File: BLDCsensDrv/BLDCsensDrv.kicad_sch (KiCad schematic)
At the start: 31 parts, among them J1 Screw_Terminal_01x02, J3 Screw_Terminal_01x03, Q1 IRF540N, Q2 IRF540N, Q3 IRF540N, Q4 IRF540N, Q5 IRF540N, Q6 IRF540N, U1 MCT8329A1IREER

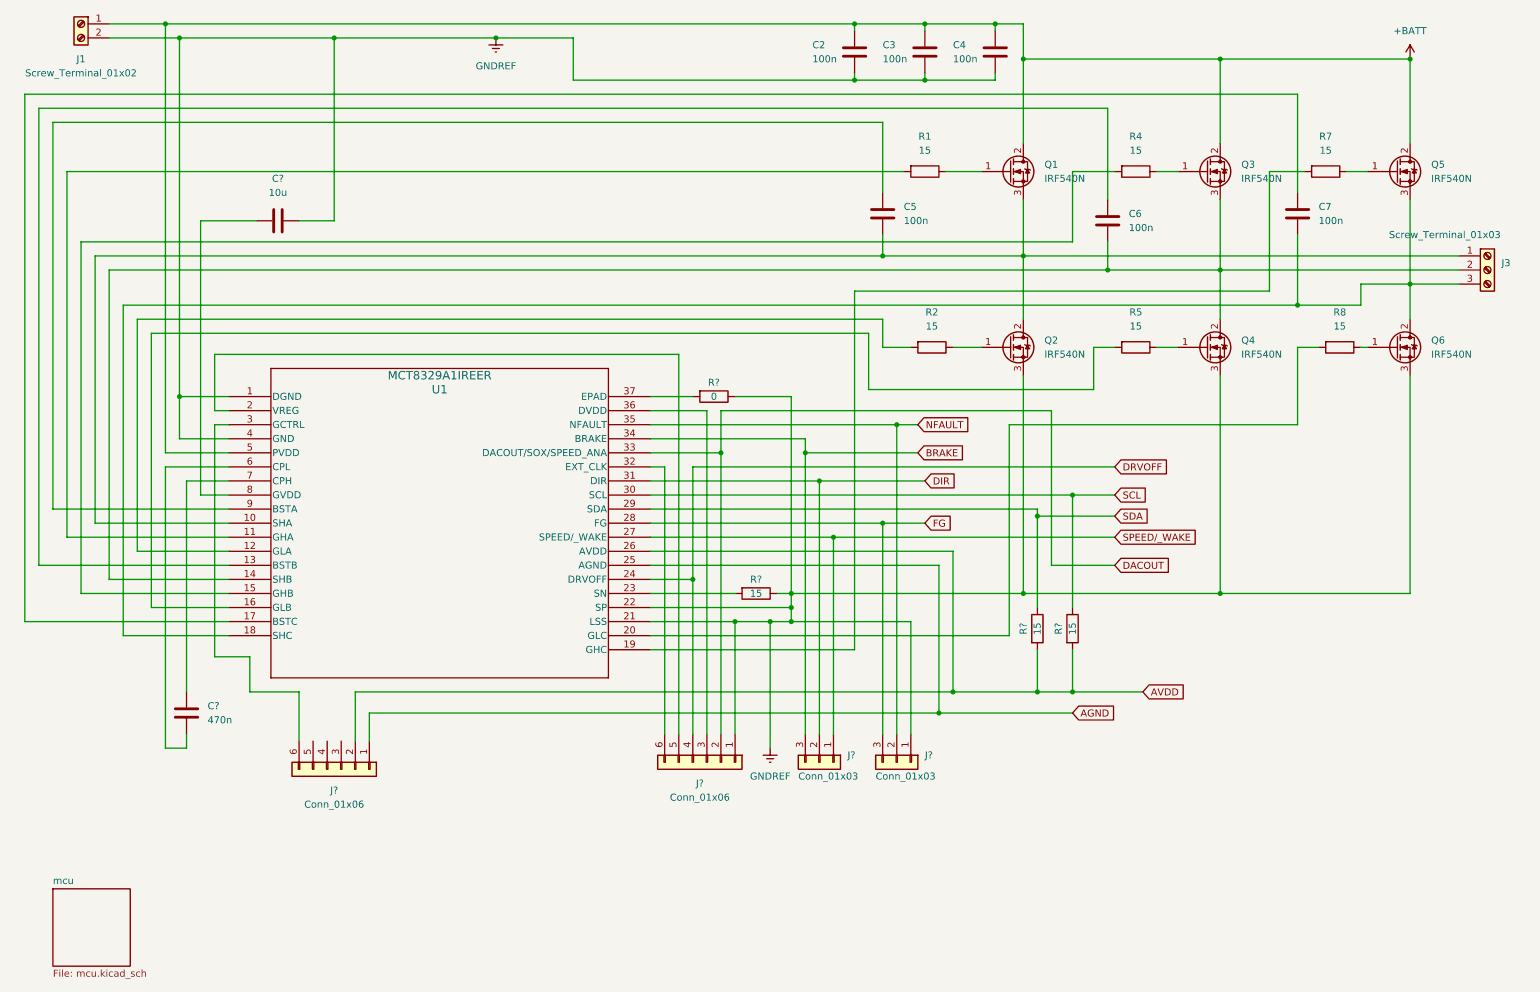
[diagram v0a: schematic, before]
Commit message: 3-phase Trapezoidal Control hardware ready for prototype prod.
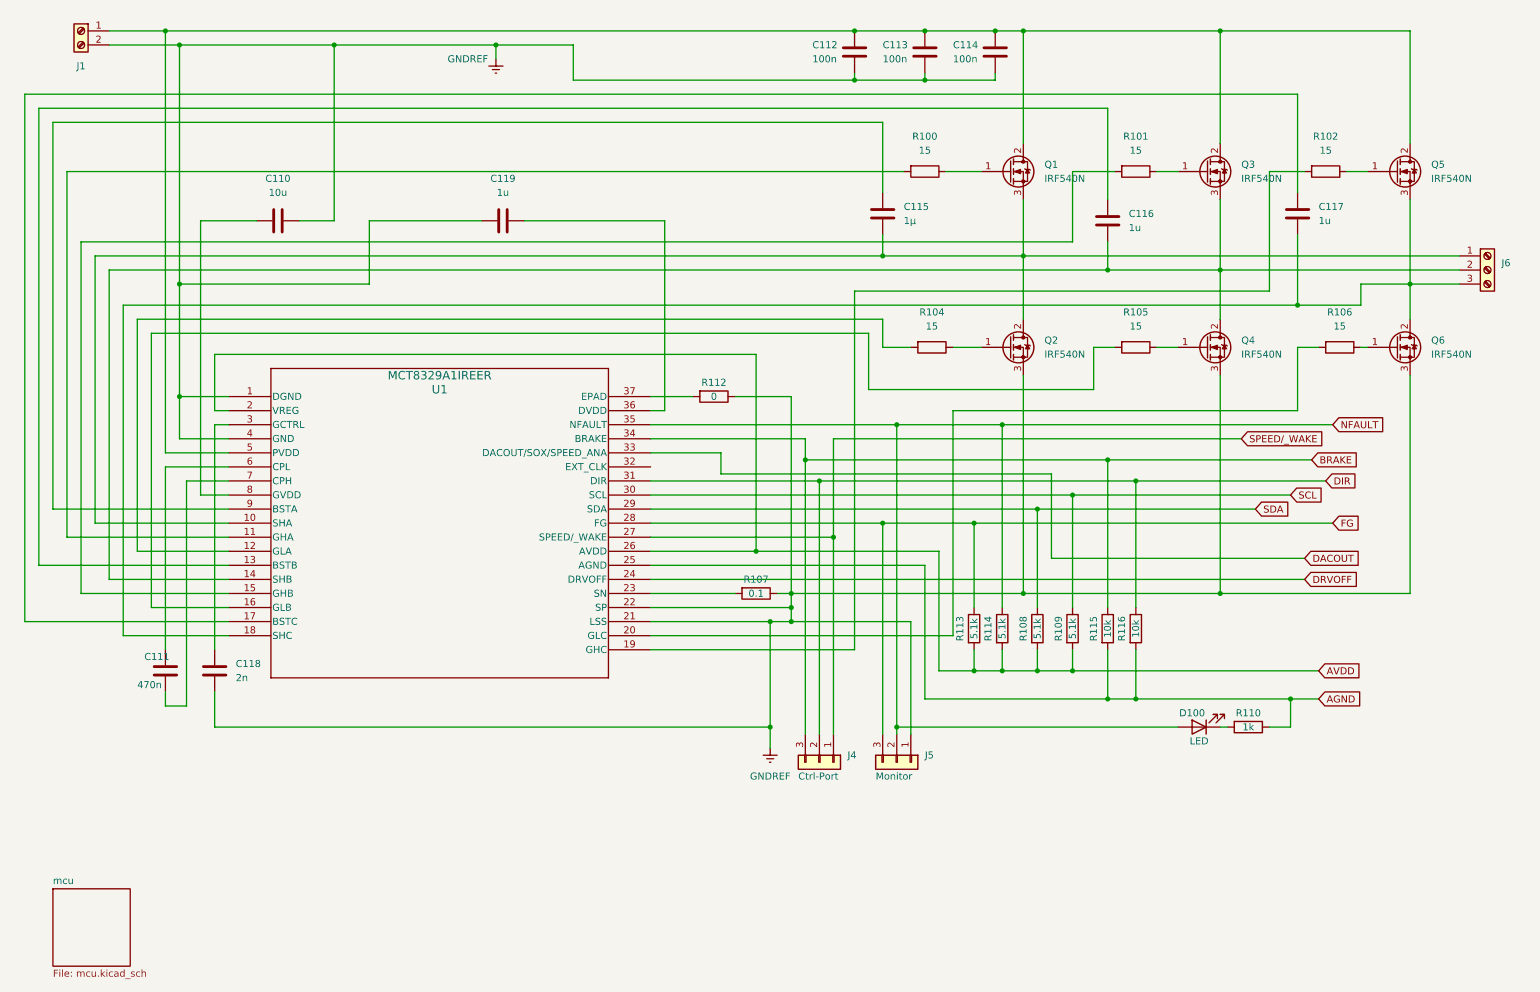
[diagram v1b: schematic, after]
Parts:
- removed C?: 470n, Capacitor_THT:C_Axial_L3.8mm_D2.6mm_P7.50mm_Horizontal, symbol Device:C
- removed J? (x2): Conn_01x06, symbol Connector_Generic:Conn_01x06
- added C111: 470n, Capacitor_SMD:C_1206_3216Metric_Pad1.33x1.80mm_HandSolder, symbol Device:C
- added C118: 2n, Capacitor_SMD:C_1206_3216Metric_Pad1.33x1.80mm_HandSolder, symbol Device:C
- added C119: 1u, Capacitor_SMD:C_1206_3216Metric_Pad1.33x1.80mm_HandSolder, symbol Device:C
- added D100: LED, LED_SMD:LED_1206_3216Metric_Pad1.42x1.75mm_HandSolder, symbol Device:LED
- added R110: 1k, Resistor_SMD:R_1206_3216Metric_Pad1.30x1.75mm_HandSolder, symbol Device:R
- added R113, R114: 5.1k, Resistor_SMD:R_1206_3216Metric_Pad1.30x1.75mm_HandSolder, symbol Device:R
- added R115, R116: 10k, Resistor_SMD:R_1206_3216Metric_Pad1.30x1.75mm_HandSolder, symbol Device:R
- C110: renamed from C?; footprint Capacitor_THT:C_Axial_L3.8mm_D2.6mm_P7.50mm_Horizontal -> Capacitor_SMD:C_1206_3216Metric_Pad1.33x1.80mm_HandSolder
- C112: renamed from C2; footprint Capacitor_THT:C_Axial_L3.8mm_D2.6mm_P7.50mm_Horizontal -> Capacitor_SMD:C_1206_3216Metric_Pad1.33x1.80mm_HandSolder
- C113: renamed from C3; footprint Capacitor_THT:C_Axial_L3.8mm_D2.6mm_P7.50mm_Horizontal -> Capacitor_SMD:C_1206_3216Metric_Pad1.33x1.80mm_HandSolder
- C114: renamed from C4; footprint Capacitor_THT:C_Axial_L3.8mm_D2.6mm_P7.50mm_Horizontal -> Capacitor_SMD:C_1206_3216Metric_Pad1.33x1.80mm_HandSolder
- C115: renamed from C5; value 100n -> 1µ; footprint Capacitor_THT:C_Axial_L3.8mm_D2.6mm_P7.50mm_Horizontal -> Capacitor_SMD:C_1206_3216Metric_Pad1.33x1.80mm_HandSolder
- C116: renamed from C6; value 100n -> 1u; footprint Capacitor_THT:C_Axial_L3.8mm_D2.6mm_P7.50mm_Horizontal -> Capacitor_SMD:C_1206_3216Metric_Pad1.33x1.80mm_HandSolder
- C117: renamed from C7; value 100n -> 1u; footprint Capacitor_THT:C_Axial_L3.8mm_D2.6mm_P7.50mm_Horizontal -> Capacitor_SMD:C_1206_3216Metric_Pad1.33x1.80mm_HandSolder
- J4: renamed from J?; value Conn_01x03 -> Ctrl-Port; footprint (none) -> Connector_PinHeader_2.54mm:PinHeader_1x03_P2.54mm_Vertical
- J5: renamed from J?; value Conn_01x03 -> Monitor; footprint (none) -> Connector_PinHeader_2.54mm:PinHeader_1x03_P2.54mm_Vertical
- R100: renamed from R1; footprint Resistor_THT:R_Axial_DIN0207_L6.3mm_D2.5mm_P10.16mm_Horizontal -> Resistor_SMD:R_1206_3216Metric_Pad1.30x1.75mm_HandSolder
- R101: renamed from R4; footprint Resistor_THT:R_Axial_DIN0207_L6.3mm_D2.5mm_P10.16mm_Horizontal -> Resistor_SMD:R_1206_3216Metric_Pad1.30x1.75mm_HandSolder
- R102: renamed from R7; footprint Resistor_THT:R_Axial_DIN0207_L6.3mm_D2.5mm_P10.16mm_Horizontal -> Resistor_SMD:R_1206_3216Metric_Pad1.30x1.75mm_HandSolder
- R104: renamed from R2; footprint Resistor_THT:R_Axial_DIN0207_L6.3mm_D2.5mm_P10.16mm_Horizontal -> Resistor_SMD:R_1206_3216Metric_Pad1.30x1.75mm_HandSolder
- R105: renamed from R5; footprint Resistor_THT:R_Axial_DIN0207_L6.3mm_D2.5mm_P10.16mm_Horizontal -> Resistor_SMD:R_1206_3216Metric_Pad1.30x1.75mm_HandSolder
- R106: renamed from R8; footprint Resistor_THT:R_Axial_DIN0207_L6.3mm_D2.5mm_P10.16mm_Horizontal -> Resistor_SMD:R_1206_3216Metric_Pad1.30x1.75mm_HandSolder
- R107: renamed from R?; value 15 -> 0.1; footprint Resistor_THT:R_Axial_DIN0207_L6.3mm_D2.5mm_P10.16mm_Horizontal -> Resistor_SMD:R_1206_3216Metric_Pad1.30x1.75mm_HandSolder
- R108, R109: renamed from R?; value 15 -> 5.1k; footprint Resistor_THT:R_Axial_DIN0207_L6.3mm_D2.5mm_P10.16mm_Horizontal -> Resistor_SMD:R_1206_3216Metric_Pad1.30x1.75mm_HandSolder
- R112: renamed from R?; footprint Resistor_THT:R_Axial_DIN0207_L6.3mm_D2.5mm_P10.16mm_Horizontal -> Resistor_SMD:R_1206_3216Metric_Pad1.30x1.75mm_HandSolder
- renumbered J3 to J6
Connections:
- net AGND: now also R110.1, R115.2, R116.2
- net AVDD: now also U1.2 (VREG), R113.2, R114.2
- net BRAKE: now also R115.1
- net DIR: now also R116.1
- net FG: now also R113.1
- net GNDREF: now also C118.2, C119.1
- net NFAULT: now also D100.2 (A), R114.1
- net at U1.7 (CPH): now also C111.2
- net at U1.6 (CPL): now also C111.1
- net at U1.3 (GCTRL): now also C118.1
- net at U1.36 (DVDD): now also C119.2
- net +BATT: no longer names the net of C112.1, C113.1, C114.1, J1.1 (Pin_1), Q1.2 (D), Q3.2 (D), Q5.2 (D), U1.5 (PVDD)
- new net: D100.1 (K), R110.2
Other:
- moved on the sheet: J1

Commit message: Hasty checkin of current development projects...
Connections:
- net PVDD: now reaches C112.1, C113.1, C114.1, J1.1 (Pin_1), Q1.2 (D), Q3.2 (D), Q5.2 (D), U1.5 (PVDD)
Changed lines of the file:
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@@
+	)
+	(junction
+		(at 40.64 27.94)
+		(diameter 0)
+		(color 0 0 0 0)
 	)
 	(junction
@@
 	(wire
 		(pts
+			(xy 36.83 27.94) (xy 40.64 27.94)
+		)
+		(stroke
+			(width 0)
+			(type default)
+		)
+	)
+	(wire
+		(pts
 			(xy 149.86 127) (xy 149.86 146.05)
 		)
@@
 	(wire
 		(pts
+			(xy 40.64 27.94) (xy 40.64 20.32)
+		)
+		(stroke
+			(width 0)
+			(type default)
+		)
+	)
+	(wire
+		(pts
 			(xy 128.27 132.08) (xy 165.1 132.08)
 		)
@@
 	(wire
 		(pts
-			(xy 40.64 96.52) (xy 40.64 20.32)
+			(xy 40.64 96.52) (xy 40.64 27.94)
 		)
 		(stroke
@@
 				(hide yes)
 			)
+		)
+	)
+	(global_label "PVDD"
+		(shape input)
+		(at 36.83 27.94 180)
+		(fields_autoplaced yes)
+		(effects
+			(font
+				(size 1.27 1.27)
+			)
+			(justify right)
+		)
+		(property "Intersheetrefs" "${INTERSHEET_REFS}"
+			(at 28.9462 27.94 0)
+			(effects
+				(font
+					(size 1.27 1.27)
+				)
+				(justify right)
+				(hide yes)
+			)
